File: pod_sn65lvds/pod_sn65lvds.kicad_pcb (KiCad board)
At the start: 4 copper layers, 48 x 32 mm, 32 parts, among them J1 HDMI_A, J2 Conn_02x04_Odd_Even, U1 SN65LVDS047PW, U2 TLV74325PDBVR

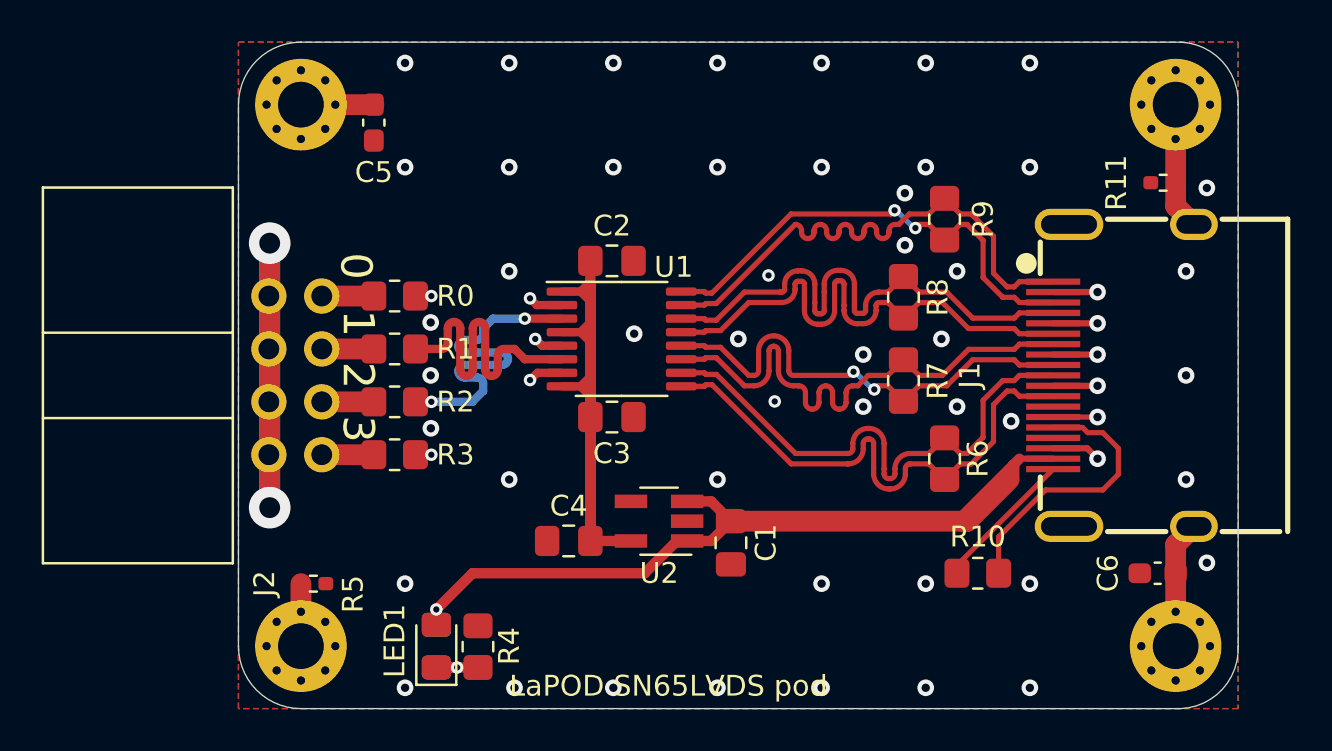
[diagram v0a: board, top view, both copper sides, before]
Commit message: fix: Replace SN65LVDS31D/SN65LVDS047W with SN65LVDS391PWR
We accidentally used the incorrect LVDS comparator. The difference is
subtle, but important.

The symbol came from the KiCad default library, the rest of the part
number from LCSC, but was simply the wrong one. 31D vs 391PWR. Subtle
but important.

Luckily, the footprint was almost the same, so no real changes where needed
here.

Signed-off-by: Olliver Schinagl <oliver@schinagl.nl>
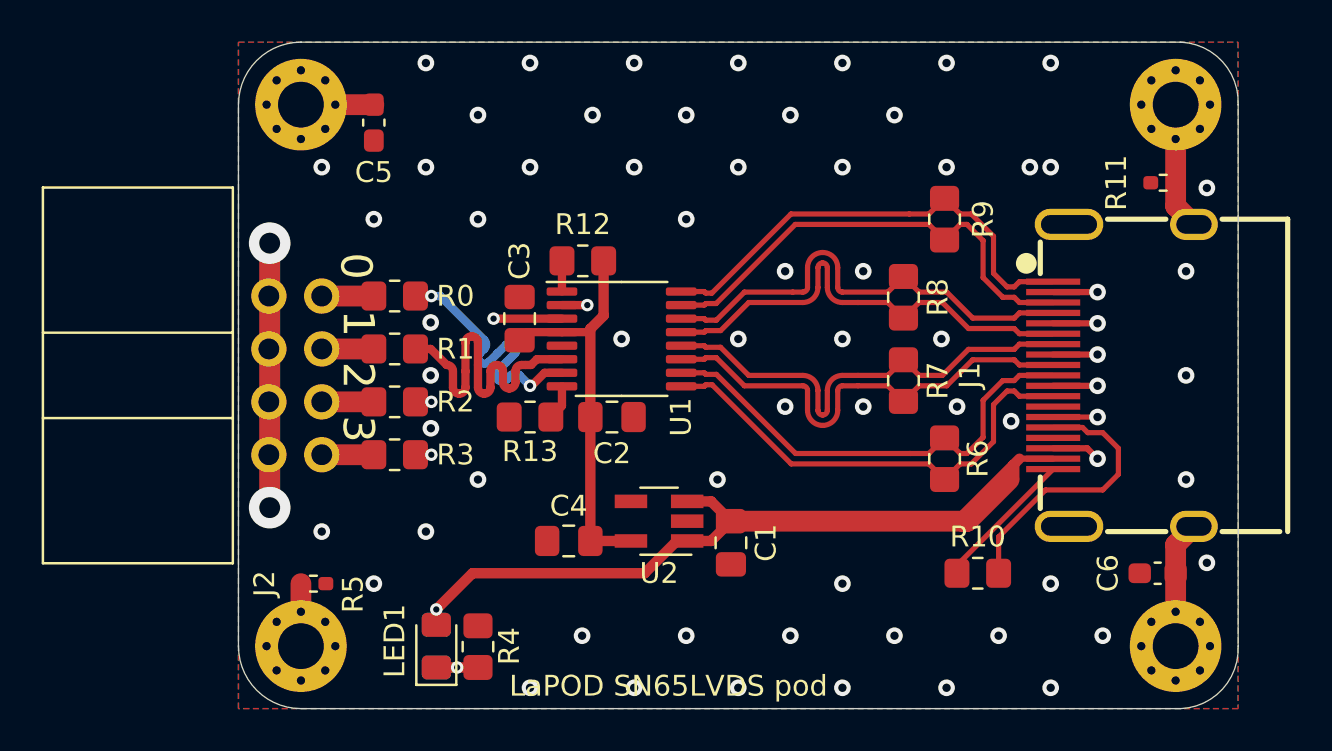
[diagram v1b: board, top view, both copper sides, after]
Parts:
- added R12: 1 kΩ, Resistor_SMD:R_0805_2012Metric_Pad1.20x1.40mm_HandSolder, F.Cu at (97.5, 54.5)
- added R13: 1 kΩ, Resistor_SMD:R_0805_2012Metric_Pad1.20x1.40mm_HandSolder, F.Cu at (95.0, 62.0)
- U1: value SN65LVDS047PW -> SN65LVDS391PWR
- moved C2 7.50 mm to (98.9, 62.0)
- moved C3 6.48 mm to (94.5, 57.3), turned to 90 degrees
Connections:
- U1 pad 1: +3V3 -> Net-(U1-EN1,2)
- U1 pad 11: OUT1+ -> OUT1-
- U1 pad 12: OUT1- -> OUT1+
- U1 pad 15: OUT3+ -> OUT3-
- U1 pad 16: OUT3- -> OUT3+
- U1 pad 8: +3V3 -> Net-(U1-EN3,4)
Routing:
- net +3V3: track 34.1 -> 19.1 mm
- net OUT2-: track 26.1 -> 22.6 mm
- net OUT2+: track 26.1 -> 22.6 mm
- net OUT1+: track 26.1 -> 22.6 mm
- net OUT0+: track 26.2 -> 22.7 mm
- net OUT0-: track 26.2 -> 22.7 mm
- net OUT3+: track 26.1 -> 22.7 mm
- net IN0: track 16.0 -> 13.2 mm
- net Net-(U1-EN3,4): track 0.00 -> 1.70 mm
- net Net-(U1-EN1,2): track 0.00 -> 1.48 mm
- net GND: track 39.8 -> 38.4 mm, vias 57 -> 69
- net OUT1-: track 23.1 -> 22.6 mm, vias 2 -> 0
- net OUT3-: track 23.2 -> 22.7 mm, vias 2 -> 0
